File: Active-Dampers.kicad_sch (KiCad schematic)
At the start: 16 parts, among them IC6 MCP25625-E_ML, J9 M50-3630242R, U1 ESP32-S3-WROOM-1, U2 DRV8848, U3 DRV8848, U4 L80-R, Y3 X50328MSB2GI

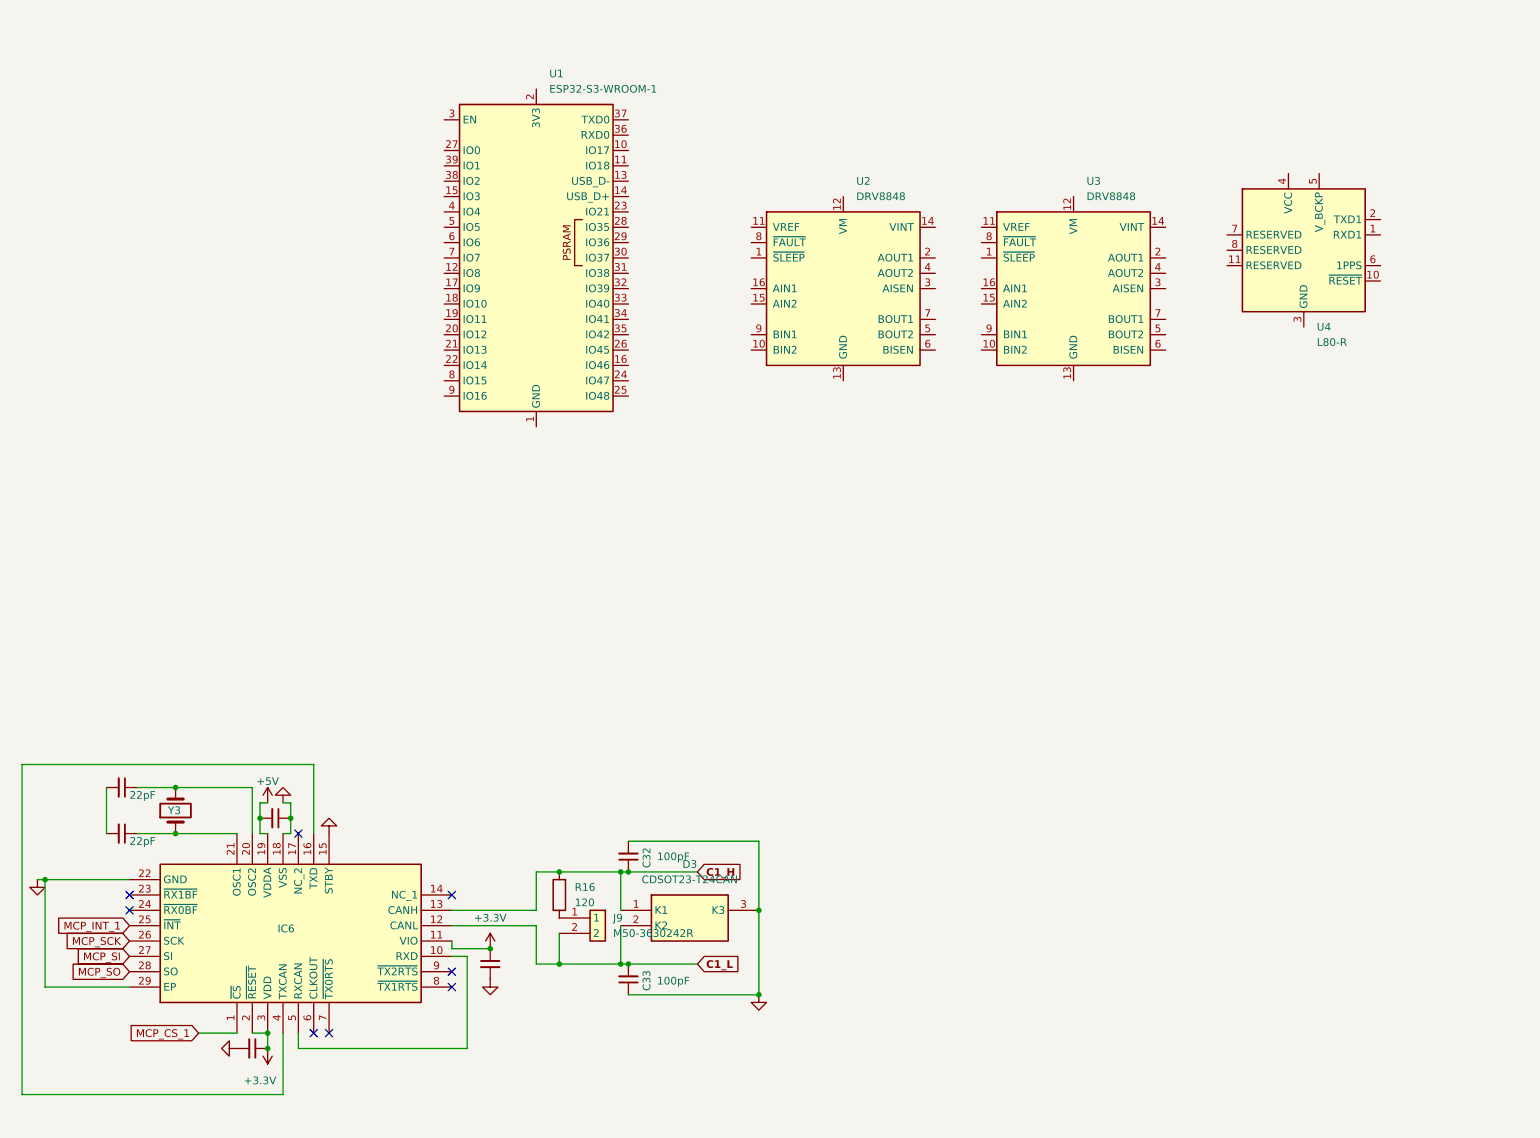
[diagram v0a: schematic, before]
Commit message: redo design to esp32
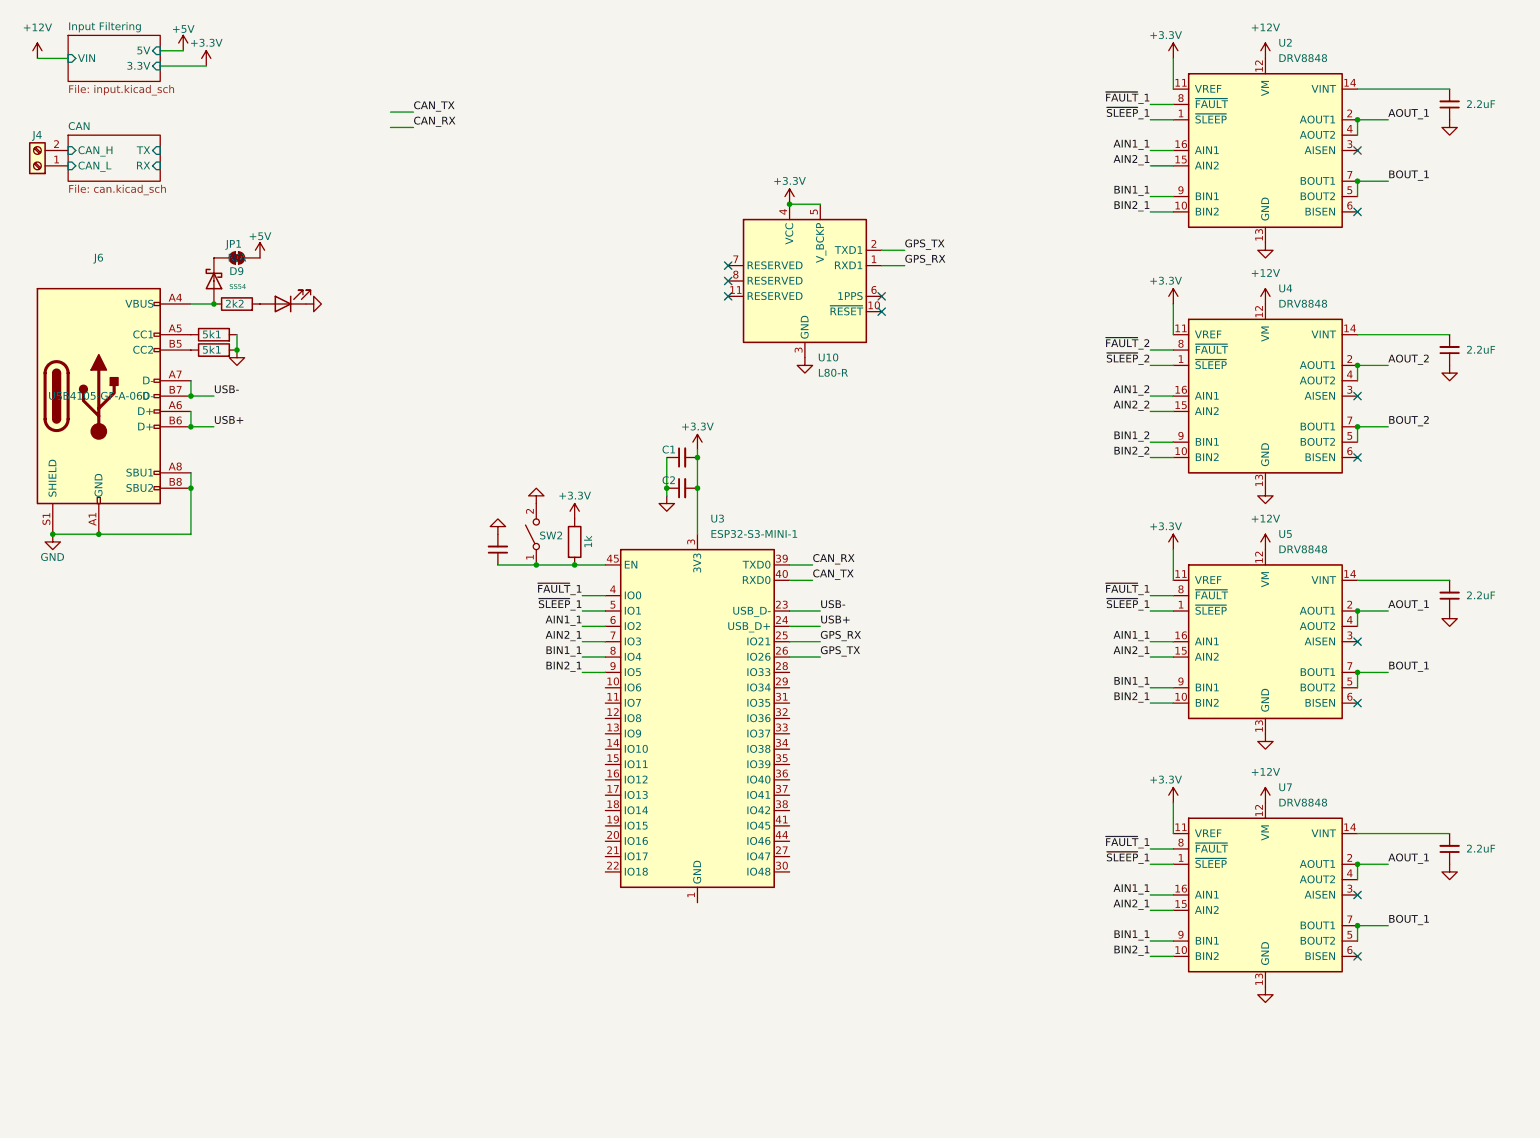
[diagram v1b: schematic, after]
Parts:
- removed C32, C33: 100pF, PCM_Capacitor_SMD_AKL:C_0402_1005Metric, symbol Device:C_Small
- removed C36, C37: 22pF, PCM_Capacitor_SMD_AKL:C_0402_1005Metric, symbol Device:C_Small
- removed C38, C39, C40: 0.1uF, PCM_Capacitor_SMD_AKL:C_0402_1005Metric, symbol Device:C_Small
- removed D3: CDSOT23-T24CAN, SamacSys_Parts:SOT95P230X117-3N, symbol SamacSys_Parts:CDSOT23-T24CAN
- removed IC6: MCP25625-E_ML, SamacSys_Parts:QFN65P600X600X100-29N-D, symbol SamacSys_Parts:MCP25625-E_ML
- removed J9: M50-3630242R, SamacSys_Parts:M503630242R, symbol SamacSys_Parts:M50-3630242R
- removed R16: 120, PCM_Resistor_SMD_AKL:R_0402_1005Metric, symbol Device:R
- removed U1: ESP32-S3-WROOM-1, RF_Module:ESP32-S3-WROOM-1, symbol RF_Module:ESP32-S3-WROOM-1
- removed U3: DRV8848, Package_SO:TSSOP-16-1EP_4.4x5mm_P0.65mm, symbol Driver_Motor:DRV8848
- removed U4: L80-R, RF_GPS:Quectel_L80-R, symbol RF_GPS:L80-R
- removed Y3: X50328MSB2GI, Crystal:Crystal_SMD_5032-2Pin_5.0x3.2mm, symbol Device:Crystal
- added C1: 1uF, PCM_Capacitor_SMD_AKL:C_0402_1005Metric, symbol Device:C_Small
- added C2, C22: 10uF, PCM_Capacitor_SMD_AKL:C_0402_1005Metric, symbol Device:C_Small
- added C20, C21, C23, C24: 2.2uF, PCM_Capacitor_SMD_AKL:C_0402_1005Metric, symbol Device:C_Small
- added D8: LED BLUE, PCM_LED_SMD_AKL:LED_0402_1005Metric, symbol Device:LED
- added D9: SS54, PCM_JLCPCB:D_SMA, symbol PCM_JLCPCB-Diodes:Schottky,SS54
- added J4: Conn_01x02, TerminalBlock_Phoenix:TerminalBlock_Phoenix_MPT-0,5-2-2.54_1x02_P2.54mm_Horizontal, symbol Connector:Screw_Terminal_01x02
- added J6: USB_C_Receptacle_USB2.0_16P, Connector_USB:USB_C_Receptacle_HRO_TYPE-C-31-M-12, symbol Connector:USB_C_Receptacle_USB2.0_16P
- added JP1: SolderJumper_2_Bridged, Jumper:SolderJumper-2_P1.3mm_Bridged_Pad1.0x1.5mm, symbol Jumper:SolderJumper_2_Bridged
- added R23: 1k, PCM_Resistor_SMD_AKL:R_0402_1005Metric, symbol Device:R
- added R6, R7: 5k1, PCM_Resistor_SMD_AKL:R_0402_1005Metric, symbol Device:R
- added R8: 2k2, PCM_Resistor_SMD_AKL:R_0402_1005Metric, symbol Device:R
- added SW2: SW_SPST, Button_Switch_SMD:SW_SPST_TS-1088-xR025, symbol Switch:SW_SPST
- added U10: L80-R, RF_GPS:Quectel_L80-R, symbol RF_GPS:L80-R
- added U3: ESP32-S3-MINI-1, RF_Module:ESP32-S2-MINI-1, symbol RF_Module:ESP32-S3-MINI-1
- added U4, U5, U7: DRV8848, Package_SO:TSSOP-16-1EP_4.4x5mm_P0.65mm, symbol Driver_Motor:DRV8848
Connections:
- net +3.3V: now also U2.11 (VREF), C1.2, C2.2, R23.1, U10.4 (VCC), U10.5 (V_BCKP), U3.3 (3V3), U4.11 (VREF), U5.11 (VREF), U7.11 (VREF)
- net +5V: now also JP1.2 (B)
- net GND: now also U2.13 (GND), U2.17 (GND), C1.1, C2.1, C20.1, C21.1, C22.2, C23.1, C24.1, D8.1 (K), J6.A1 (GND), J6.A12 (GND), J6.A8 (SBU1), J6.B1 (GND), J6.B12 (GND), J6.B8 (SBU2), J6.S1 (SHIELD), R6.2, R7.2, SW2.2 (B), U10.12 (GND), U10.3 (GND), U4.13 (GND), U4.17 (GND), U5.13 (GND), U5.17 (GND), U7.13 (GND), U7.17 (GND)
- net ~{SLEEP}_1: now reaches U2.1 (~{SLEEP})
- net ~{SLEEP}_1: now also U3.5 (IO1), U5.1 (~{SLEEP}), U7.1 (~{SLEEP})
- net BIN2_1: now reaches U2.10 (BIN2)
- net BIN2_1: now also U3.9 (IO5), U5.10 (BIN2), U7.10 (BIN2)
- net +12V: now reaches U2.12 (VM)
- net +12V: now also U4.12 (VM), U5.12 (VM), U7.12 (VM)
- net at U2.14 (VINT): now also C20.2
- net AIN2_1: now reaches U2.15 (AIN2)
- net AIN2_1: now also U3.7 (IO3), U5.15 (AIN2), U7.15 (AIN2)
- net AIN1_1: now reaches U2.16 (AIN1)
- net AIN1_1: now also U3.6 (IO2), U5.16 (AIN1), U7.16 (AIN1)
- net AOUT_1: now reaches U2.2 (AOUT1)
- net AOUT_1: now also U2.4 (AOUT2), U5.2 (AOUT1), U5.4 (AOUT2), U7.2 (AOUT1), U7.4 (AOUT2)
- net BOUT_1: now reaches U2.5 (BOUT2)
- net BOUT_1: now also U2.7 (BOUT1), U5.5 (BOUT2), U5.7 (BOUT1), U7.5 (BOUT2), U7.7 (BOUT1)
- net ~{FAULT}_1: now reaches U2.8 (~{FAULT})
- net ~{FAULT}_1: now also U3.4 (IO0), U5.8 (~{FAULT}), U7.8 (~{FAULT})
- net BIN1_1: now reaches U2.9 (BIN1)
- net BIN1_1: now also U3.8 (IO4), U5.9 (BIN1), U7.9 (BIN1)
- new net: C22.1, R23.2, SW2.1 (A), U3.45 (EN)
- new net: D9.2, J6.A4 (VBUS), J6.A9 (VBUS), J6.B4 (VBUS), J6.B9 (VBUS), R8.1
- new net: J6.A5 (CC1), R6.1
- new net: J6.B5 (CC2), R7.1
- new net: C23.2, U5.14 (VINT)
- new net: D9.1, JP1.1 (A)
- new net: D8.2 (A), R8.2
- new net: U3.1 (GND), U3.2 (GND), U3.42 (GND), U3.43 (GND), U3.46 (GND), U3.47 (GND), U3.48 (GND), U3.49 (GND), U3.50 (GND), U3.51 (GND), U3.52 (GND), U3.53 (GND), U3.54 (GND), U3.55 (GND), U3.56 (GND), U3.57 (GND), U3.58 (GND), U3.59 (GND), U3.60 (GND), U3.61 (GND), U3.62 (GND), U3.63 (GND), U3.64 (GND), U3.65 (GND)
- new net: C21.2, U4.14 (VINT)
- new net: C24.2, U7.14 (VINT)
- new net AIN1_2: U4.16 (AIN1)
- new net AIN2_2: U4.15 (AIN2)
- new net AOUT_2: U4.2 (AOUT1), U4.4 (AOUT2)
- new net BIN1_2: U4.9 (BIN1)
- new net BIN2_2: U4.10 (BIN2)
- new net BOUT_2: U4.5 (BOUT2), U4.7 (BOUT1)
- new net CAN/CAN_H: J4.2 (Pin_2)
- new net CAN/CAN_L: J4.1 (Pin_1)
- new net CAN_RX: U3.39 (TXD0)
- new net CAN_TX: U3.40 (RXD0)
- new net GPS_RX: U10.1 (RXD1), U3.25 (IO21)
- new net GPS_TX: U10.2 (TXD1), U3.26 (IO26)
- new net USB+: J6.A6 (D+), J6.B6 (D+), U3.24 (USB_D+)
- new net USB-: J6.A7 (D-), J6.B7 (D-), U3.23 (USB_D-)
- new net ~{FAULT}_2: U4.8 (~{FAULT})
- new net ~{SLEEP}_2: U4.1 (~{SLEEP})
- no-connect marks 8 -> 13
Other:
- added sheet CAN (can.kicad_sch)
- added sheet Input Filtering (input.kicad_sch)
- moved on the sheet: U2

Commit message: begin layout
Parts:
- added H1, H2, H3, H4: MountingHole_M3_3.2mm_Pad, MountingHole:MountingHole_2.2mm_M2_ISO14580_Pad, symbol PCM_SL_Mechanical:MountingHole_M3_3.2mm_Pad
- added J2, J3, J5, J7: Conn_01x04, Connector_JST:JST_XH_B4B-XH-AM_1x04_P2.50mm_Vertical, symbol Connector_Generic:Conn_01x04
- added J8: Barrel_Jack_Switch_Pin3Ring, Connector_BarrelJack:BarrelJack_Horizontal, symbol Connector:Barrel_Jack_Switch_Pin3Ring
- C1, C2, C20, C21, C22, C23, C24: footprint PCM_Capacitor_SMD_AKL:C_0402_1005Metric -> PCM_Capacitor_SMD_AKL:C_0603_1608Metric
- R23, R6, R7, R8: footprint PCM_Resistor_SMD_AKL:R_0402_1005Metric -> PCM_Resistor_SMD_AKL:R_0603_1608Metric
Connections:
- net +12V: now also J8.1
- net AIN1_1: no longer U5.16 (AIN1), U7.16 (AIN1)
- net AIN1_2: now also U3.12 (IO8)
- net AIN2_1: no longer U5.15 (AIN2), U7.15 (AIN2)
- net AIN2_2: now also U3.13 (IO9)
- net BIN1_1: no longer U5.9 (BIN1), U7.9 (BIN1)
- net BIN1_2: now also U3.14 (IO10)
- net BIN2_1: no longer U5.10 (BIN2), U7.10 (BIN2)
- net BIN2_2: now also U3.15 (IO11)
- net GND: now also U3.1 (GND), U3.2 (GND), U3.42 (GND), U3.43 (GND), U3.46 (GND), U3.47 (GND), U3.48 (GND), U3.49 (GND), U3.50 (GND), U3.51 (GND), U3.52 (GND), U3.53 (GND), U3.54 (GND), U3.55 (GND), U3.56 (GND), U3.57 (GND), U3.58 (GND), U3.59 (GND), U3.60 (GND), U3.61 (GND), U3.62 (GND), U3.63 (GND), U3.64 (GND), U3.65 (GND), H1.1, H2.1, H3.1, H4.1, J8.2, J8.3
- net ~{FAULT}_1: no longer U5.8 (~{FAULT}), U7.8 (~{FAULT})
- net ~{FAULT}_2: now also U3.10 (IO6)
- net ~{SLEEP}_1: no longer U5.1 (~{SLEEP}), U7.1 (~{SLEEP})
- net ~{SLEEP}_2: now also U3.11 (IO7)
- net ~{FAULT}_3: now reaches U3.16 (IO12)
- net ~{FAULT}_3: now also U5.8 (~{FAULT})
- net ~{SLEEP}_3: now reaches U3.17 (IO13)
- net ~{SLEEP}_3: now also U5.1 (~{SLEEP})
- net AIN1_3: now reaches U3.18 (IO14)
- net AIN1_3: now also U5.16 (AIN1)
- net AIN2_3: now reaches U3.19 (IO15)
- net AIN2_3: now also U5.15 (AIN2)
- net BIN1_3: now reaches U3.20 (IO16)
- net BIN1_3: now also U5.9 (BIN1)
- net BIN2_3: now reaches U3.21 (IO17)
- net BIN2_3: now also U5.10 (BIN2)
- net BIN1_4: now reaches U3.27 (IO47)
- net BIN1_4: now also U7.9 (BIN1)
- net BIN2_4: now reaches U3.30 (IO48)
- net BIN2_4: now also U7.10 (BIN2)
- net ~{FAULT}_4: now reaches U3.37 (IO41)
- net ~{FAULT}_4: now also U7.8 (~{FAULT})
- net ~{SLEEP}_4: now reaches U3.38 (IO42)
- net ~{SLEEP}_4: now also U7.1 (~{SLEEP})
- net AIN1_4: now reaches U3.41 (IO45)
- net AIN1_4: now also U7.16 (AIN1)
- net AIN2_4: now reaches U3.44 (IO46)
- net AIN2_4: now also U7.15 (AIN2)
- removed net AOUT_1: U2.2 (AOUT1), U2.4 (AOUT2), U5.2 (AOUT1), U5.4 (AOUT2), U7.2 (AOUT1), U7.4 (AOUT2)
- net AOUT_2 renamed AOUT_1_2
- net AOUT_1_2: now also U2.4 (AOUT2), J2.3 (Pin_3), J3.4 (Pin_4); no longer U4.4 (AOUT2)
- removed net BOUT_1: U2.5 (BOUT2), U2.7 (BOUT1), U5.5 (BOUT2), U5.7 (BOUT1), U7.5 (BOUT2), U7.7 (BOUT1)
- net BOUT_2 renamed BOUT_1_2
- net BOUT_1_2: now also U2.5 (BOUT2), J2.1 (Pin_1), J3.2 (Pin_2); no longer U4.5 (BOUT2)
- new net AOUT_1_1: J2.4 (Pin_4), U2.2 (AOUT1)
- new net AOUT_1_3: J5.4 (Pin_4), J7.4 (Pin_4), U5.2 (AOUT1), U7.2 (AOUT1)
- new net AOUT_2_2: J3.3 (Pin_3), U4.4 (AOUT2)
- new net AOUT_2_3: J5.3 (Pin_3), J7.3 (Pin_3), U5.4 (AOUT2), U7.4 (AOUT2)
- new net BOUT_1_1: J2.2 (Pin_2), U2.7 (BOUT1)
- new net BOUT_1_3: J5.2 (Pin_2), J7.2 (Pin_2), U5.7 (BOUT1), U7.7 (BOUT1)
- new net BOUT_2_2: J3.1 (Pin_1), U4.5 (BOUT2)
- new net BOUT_2_3: J5.1 (Pin_1), J7.1 (Pin_1), U5.5 (BOUT2), U7.5 (BOUT2)
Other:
- moved on the sheet: SW2
